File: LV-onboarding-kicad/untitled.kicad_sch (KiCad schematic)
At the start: 2 parts, among them K1 Relay_SPST-NO, U2 74LVC1G332

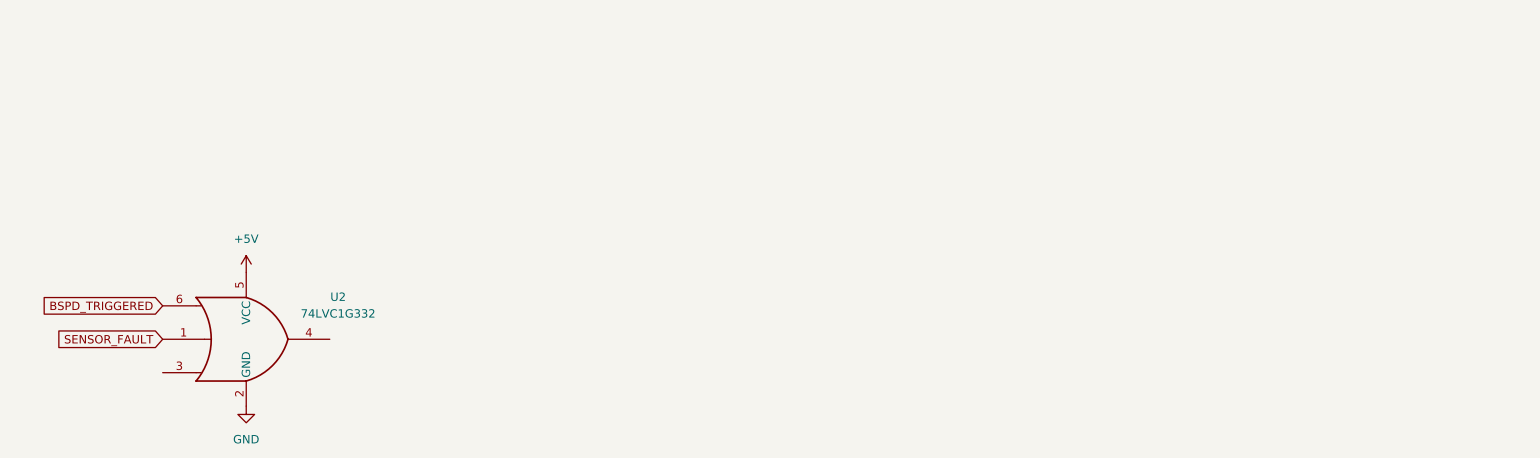
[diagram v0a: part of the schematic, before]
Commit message: BSPD research
rewatched vids from the goat ben eater for SR latch D latch and D flip flop. Added 74HC74 to schematic
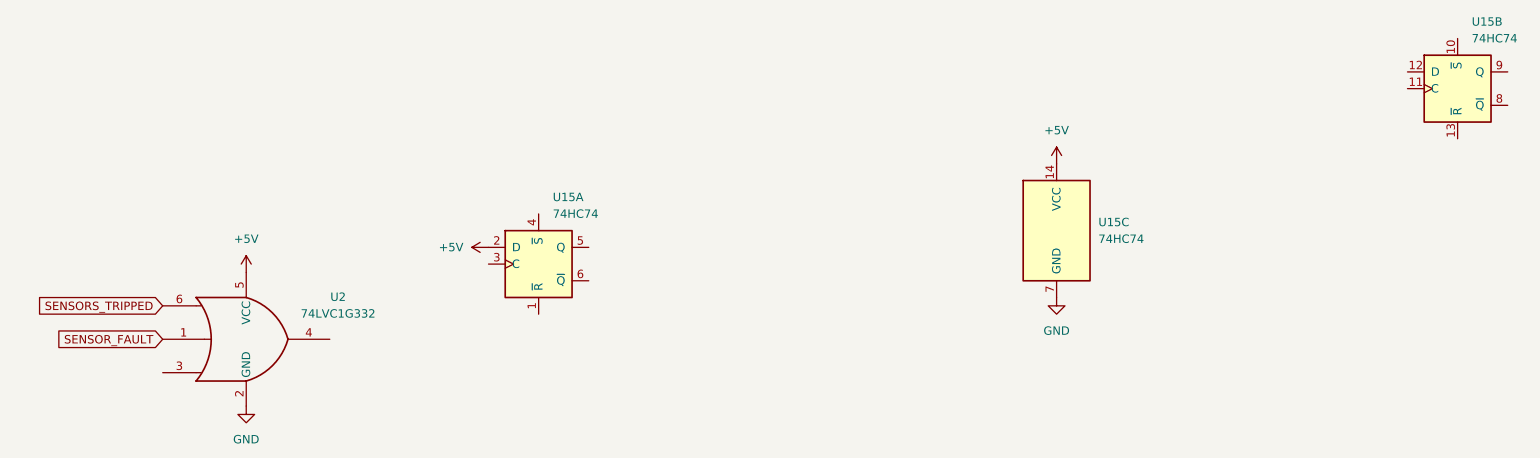
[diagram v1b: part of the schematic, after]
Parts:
- added U15: 74HC74, symbol 74xx:74HC74
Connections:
- net +5V: now also U15.14 (VCC), U15.2 (D)
- net GND: now also U15.7 (GND)
- net BSPD_TRIGGERED renamed SENSORS_TRIPPED

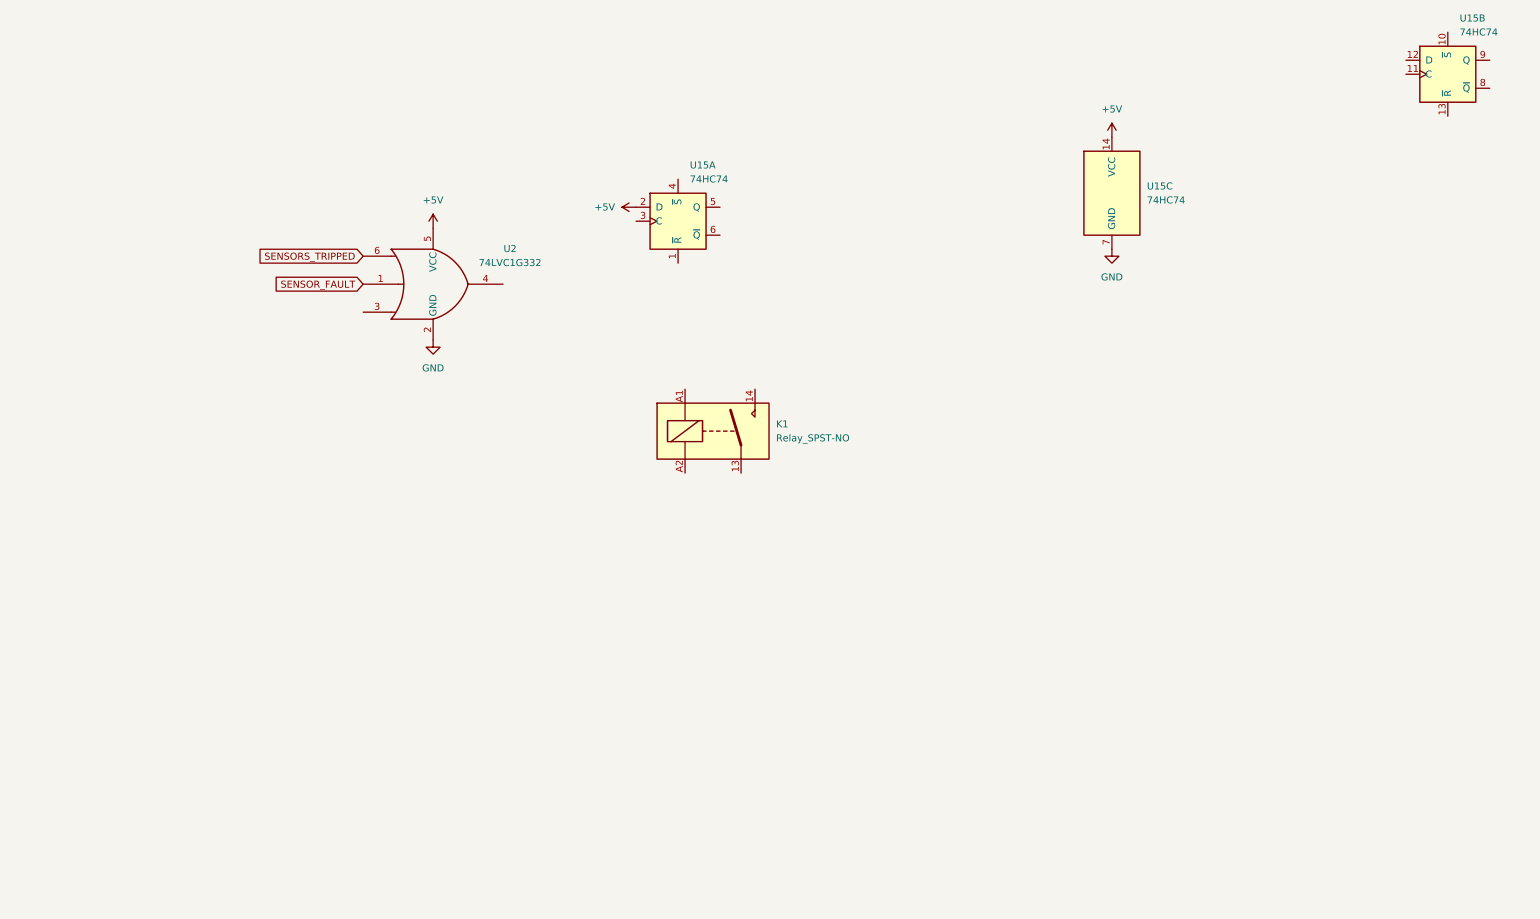
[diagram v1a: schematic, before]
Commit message: BSPD timer
forgot my timer that i needed before the  D flip flop
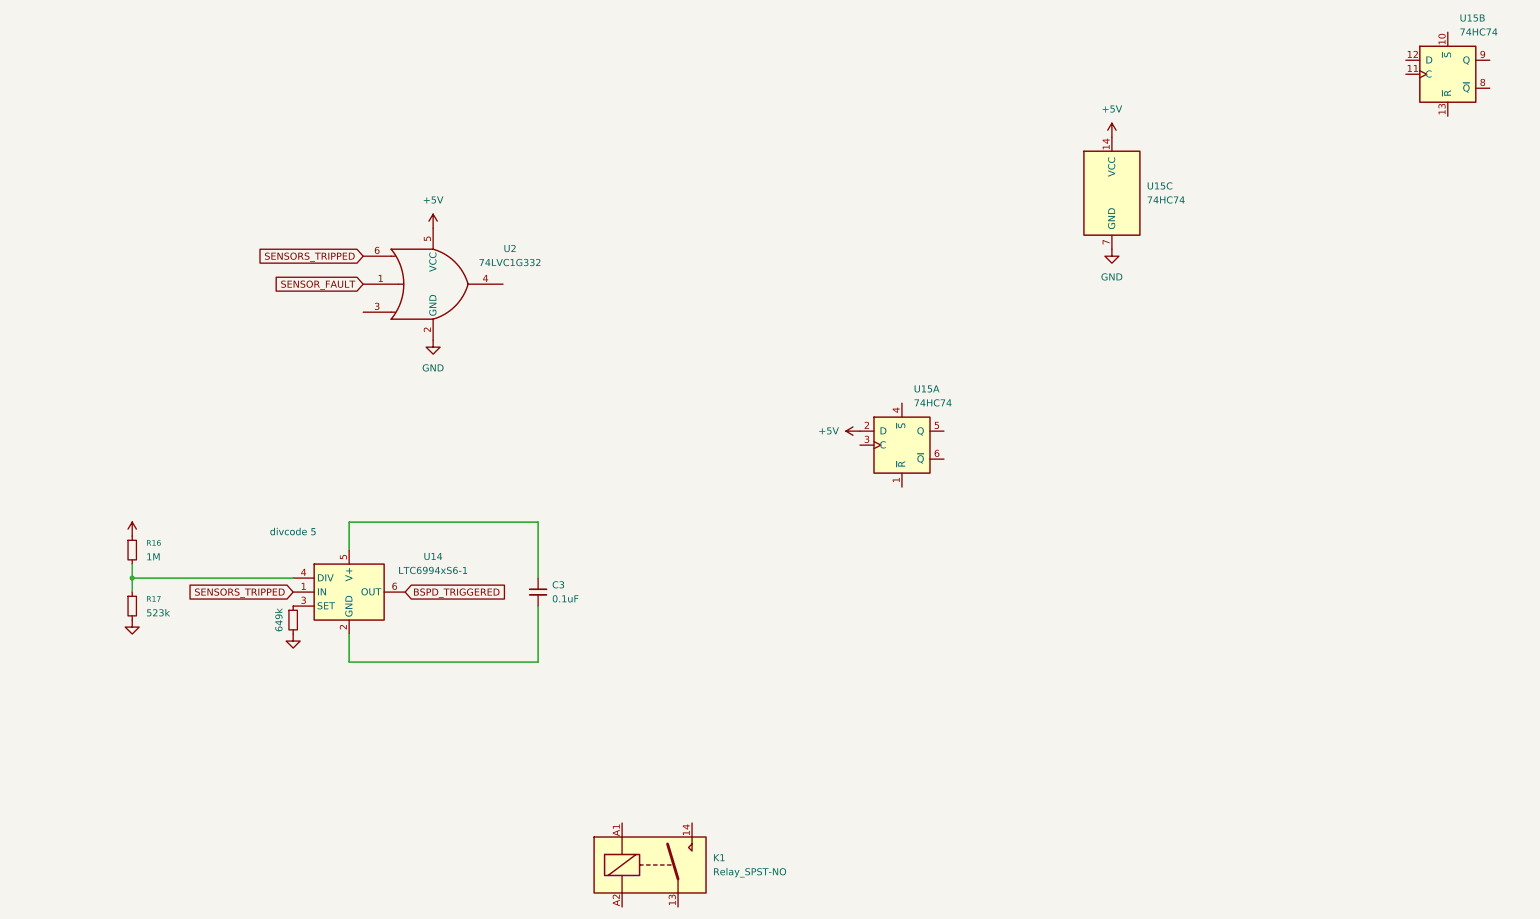
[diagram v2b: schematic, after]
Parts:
- added C3: 0.1uF, LED_SMD:LED_Kingbright_APFA3010_3x1.5mm_Horizontal, symbol Device:C_Small
- added R15: 649k, symbol Device:R_Small
- added R16: 1M, symbol Device:R_Small
- added R17: 523k, symbol Device:R_Small
- added U14: LTC6994xS6-1, Package_TO_SOT_SMD:TSOT-23-6, symbol Timer:LTC6994xS6-1
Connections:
- net +5V: now also R16.1
- net GND: now also R15.2, R17.2
- net SENSORS_TRIPPED: now also U14.1 (IN)
- new net: R16.2, R17.1, U14.4 (DIV)
- new net: R15.1, U14.3 (SET)
- new net: C3.1, U14.5 (V+)
- new net: C3.2, U14.2 (GND)
- new net BSPD_TRIGGERED: U14.6 (OUT)
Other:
- note added: "divcode 5"
- moved on the sheet: K1, U15A

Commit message: BSPD MOSFET
researched mosfets and put one in the schematic
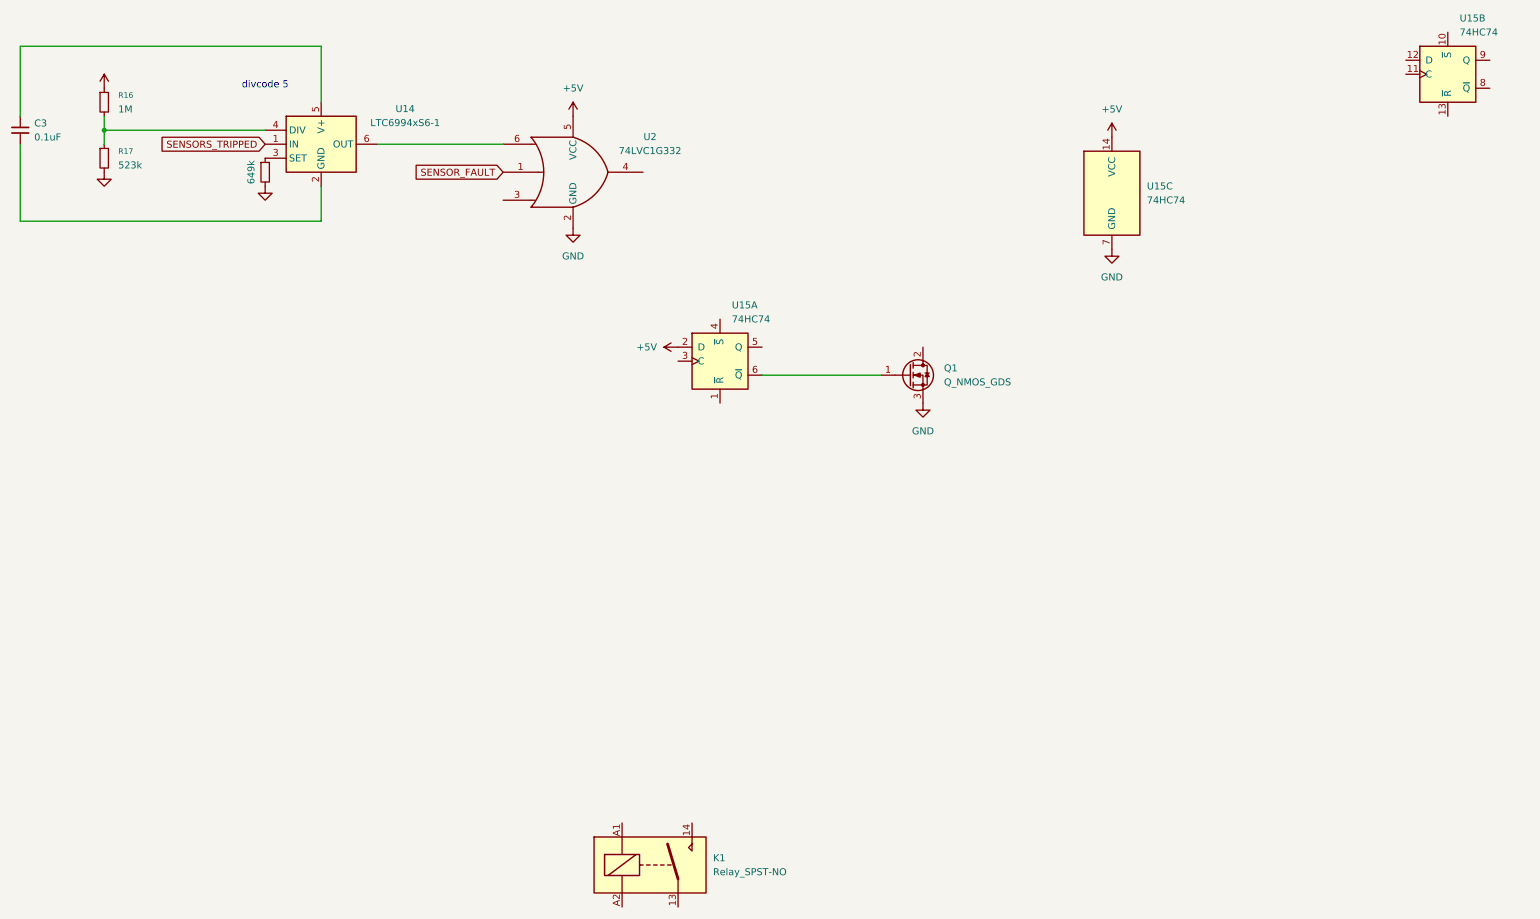
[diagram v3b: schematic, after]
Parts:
- added Q1: Q_NMOS_GDS, symbol Transistor_FET:Q_NMOS_GDS
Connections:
- net GND: now also Q1.3 (S)
- net SENSORS_TRIPPED: no longer U2.6
- net at U15.6 (~{Q}): now also Q1.1 (G)
- net BSPD_TRIGGERED: no longer names the net of U14.6 (OUT)
- net BSPD_TRIGGERED: now also U2.6
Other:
- moved on the sheet: C3, R16, R17, U14, U15A, U2

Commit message: BSPD work
luca says to replace d flip flop with SR latch still need pressure sensor values
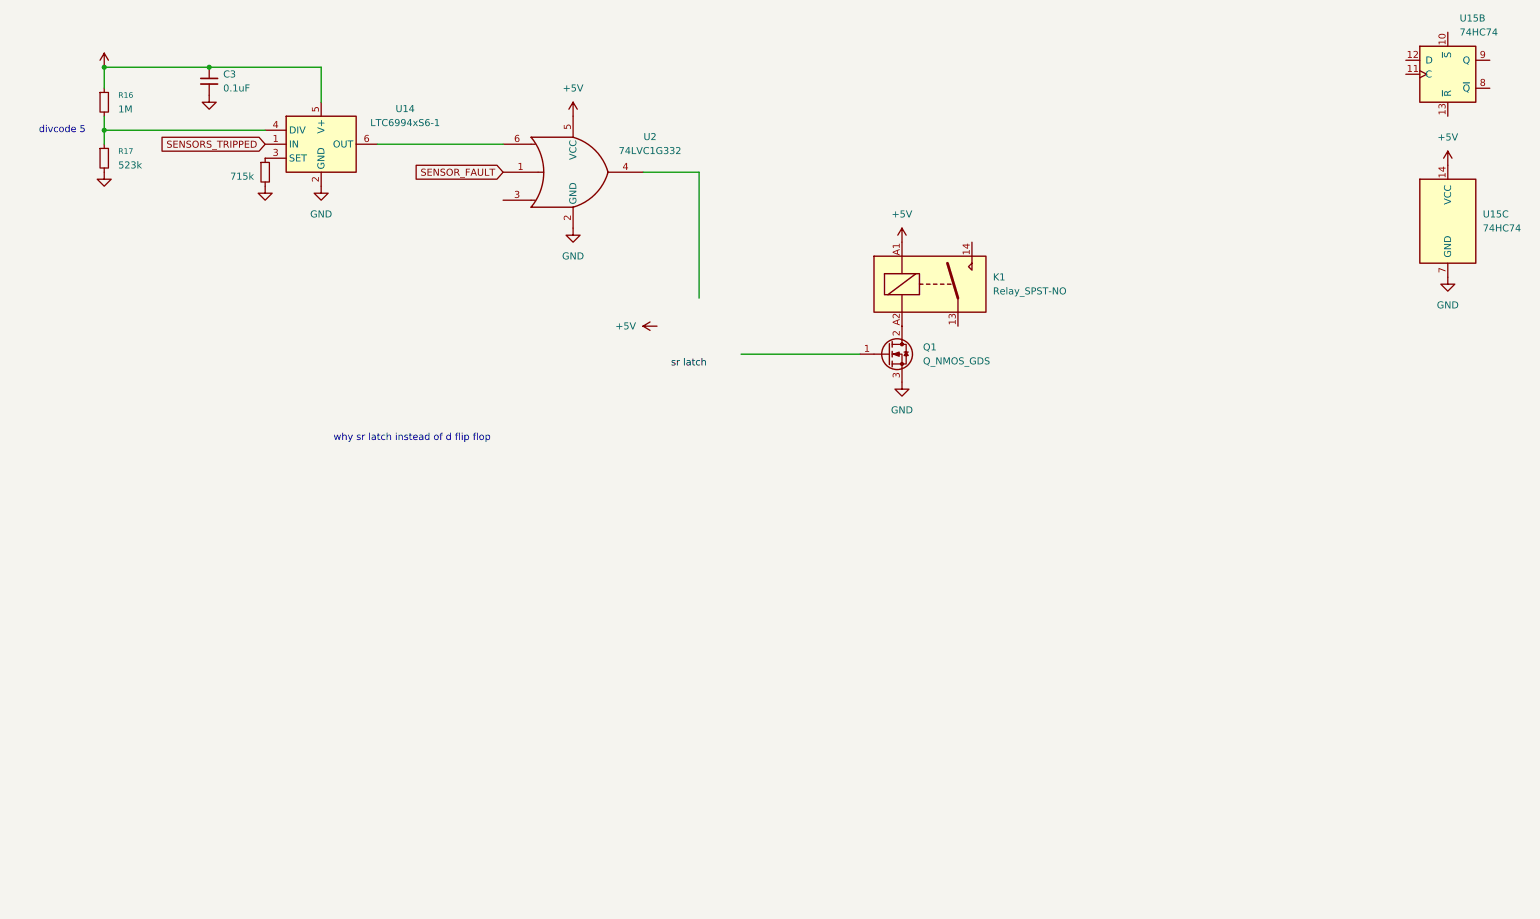
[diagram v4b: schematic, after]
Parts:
- removed unit 1 of U15
- R15: value 649k -> 715k
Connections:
- net +5V: now also C3.1, K1.A1, U14.5 (V+)
- net GND: now also C3.2, U14.2 (GND)
- net at Q1.2 (D): now also K1.A2
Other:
- note added: "why sr latch instead of d flip flop"
- moved on the sheet: C3, K1, Q1, U15C

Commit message: BSPD QOL changes
added delay block datasheet, cleaned up low and high thresholds on schematic, made SR latch, made +5v point up
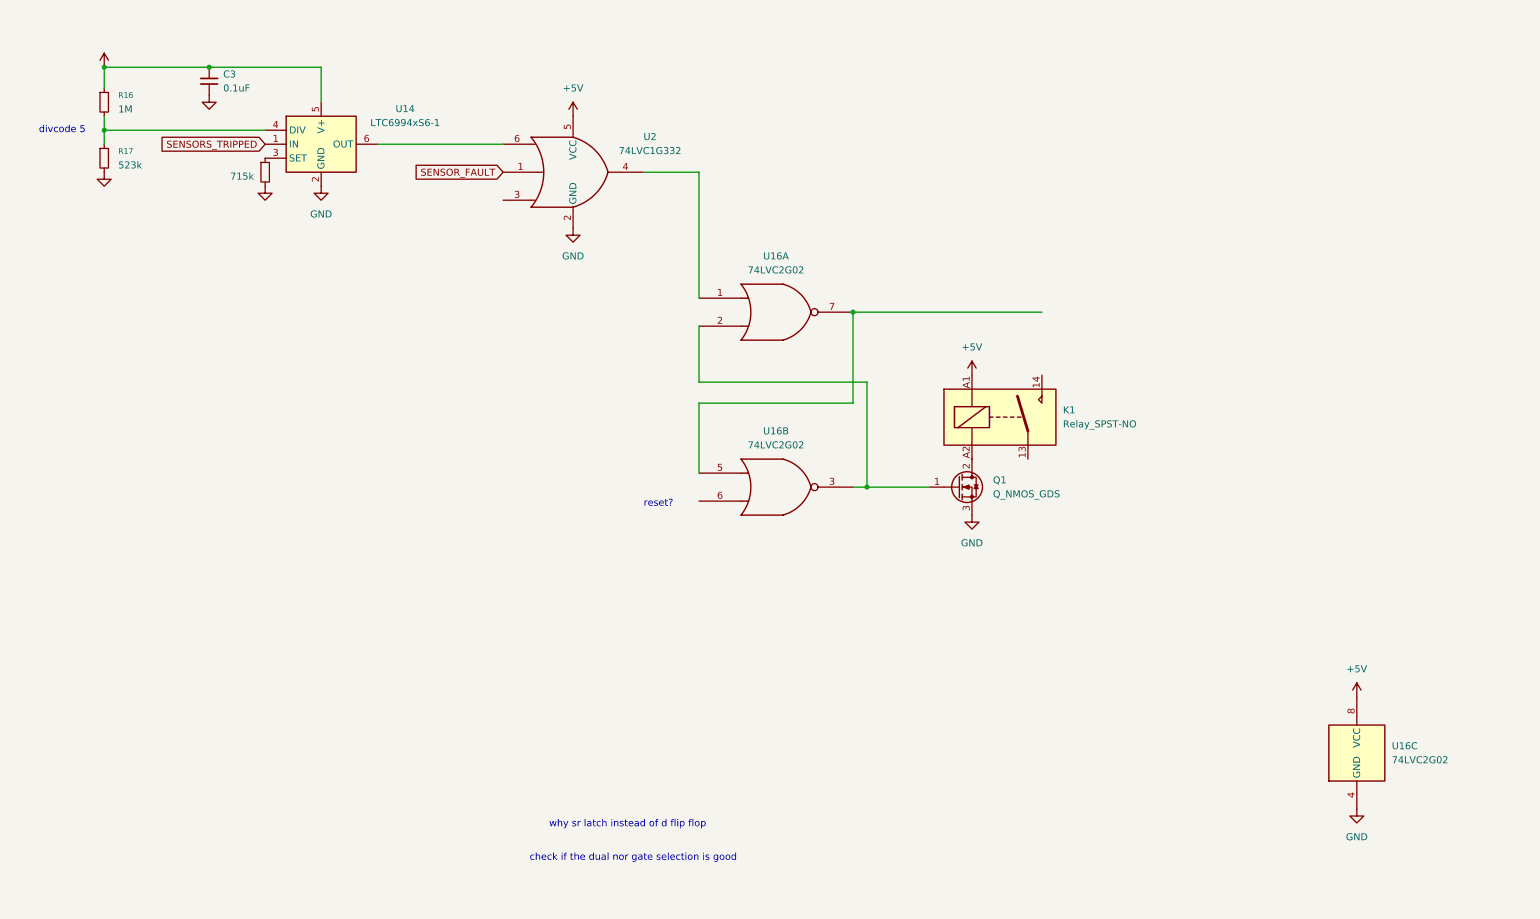
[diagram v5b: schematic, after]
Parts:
- removed U15: 74HC74, symbol 74xx:74HC74
- added U16: 74LVC2G02, symbol 74xGxx:74LVC2G02
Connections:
- net +5V: now also U16.8 (VCC)
- net GND: now also U16.4 (GND)
- net at Q1.1 (G): now also U16.2, U16.3
- net at U2.4: now also U16.1
- new net: U16.5, U16.7
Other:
- note added: "check if the dual nor gate selection is good"
- note added: "reset?"
- moved on the sheet: K1, Q1
